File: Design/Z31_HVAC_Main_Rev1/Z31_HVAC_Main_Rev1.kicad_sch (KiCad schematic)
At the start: 23 parts, among them J1 Conn_01x05, J2 Conn_02x18_Odd_Even, J3 Conn_01x10_Male, J4 Conn_01x09_Male, U1 MEGA2560PRO, U2 MCP2515, U3 TJR1443, U4 ULN2003, U5 ULN2003, U6 ULN2003, U7 ULN2003, U8 NCV4276B, U9 ULN2003

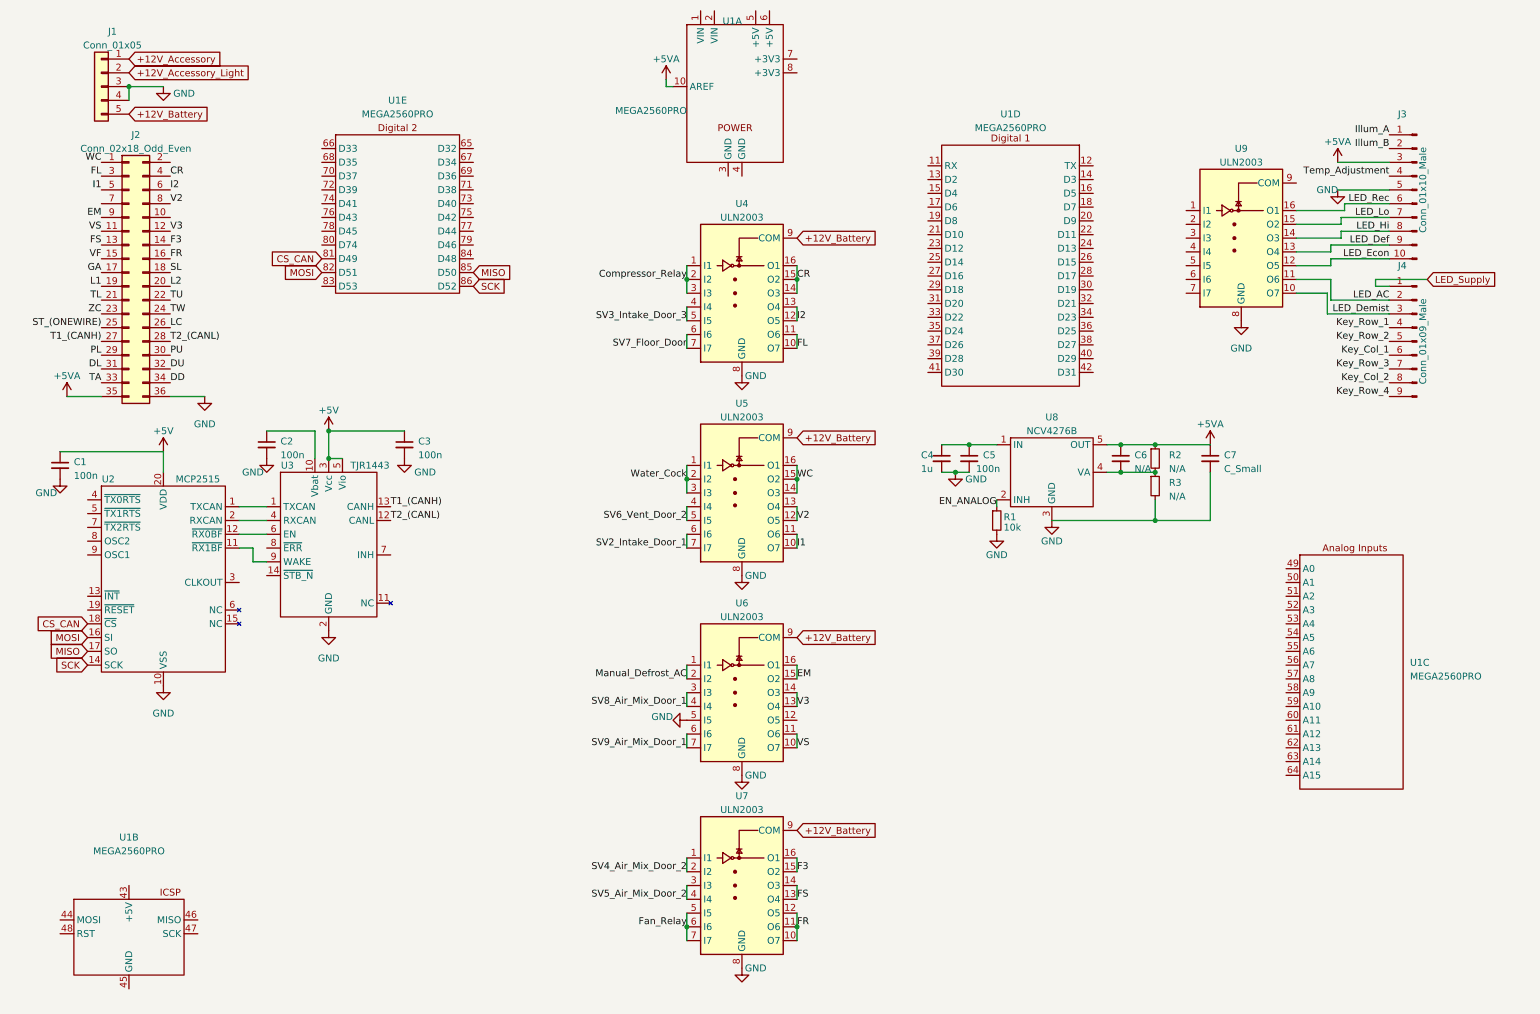
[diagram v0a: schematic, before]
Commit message: update to kicad-6
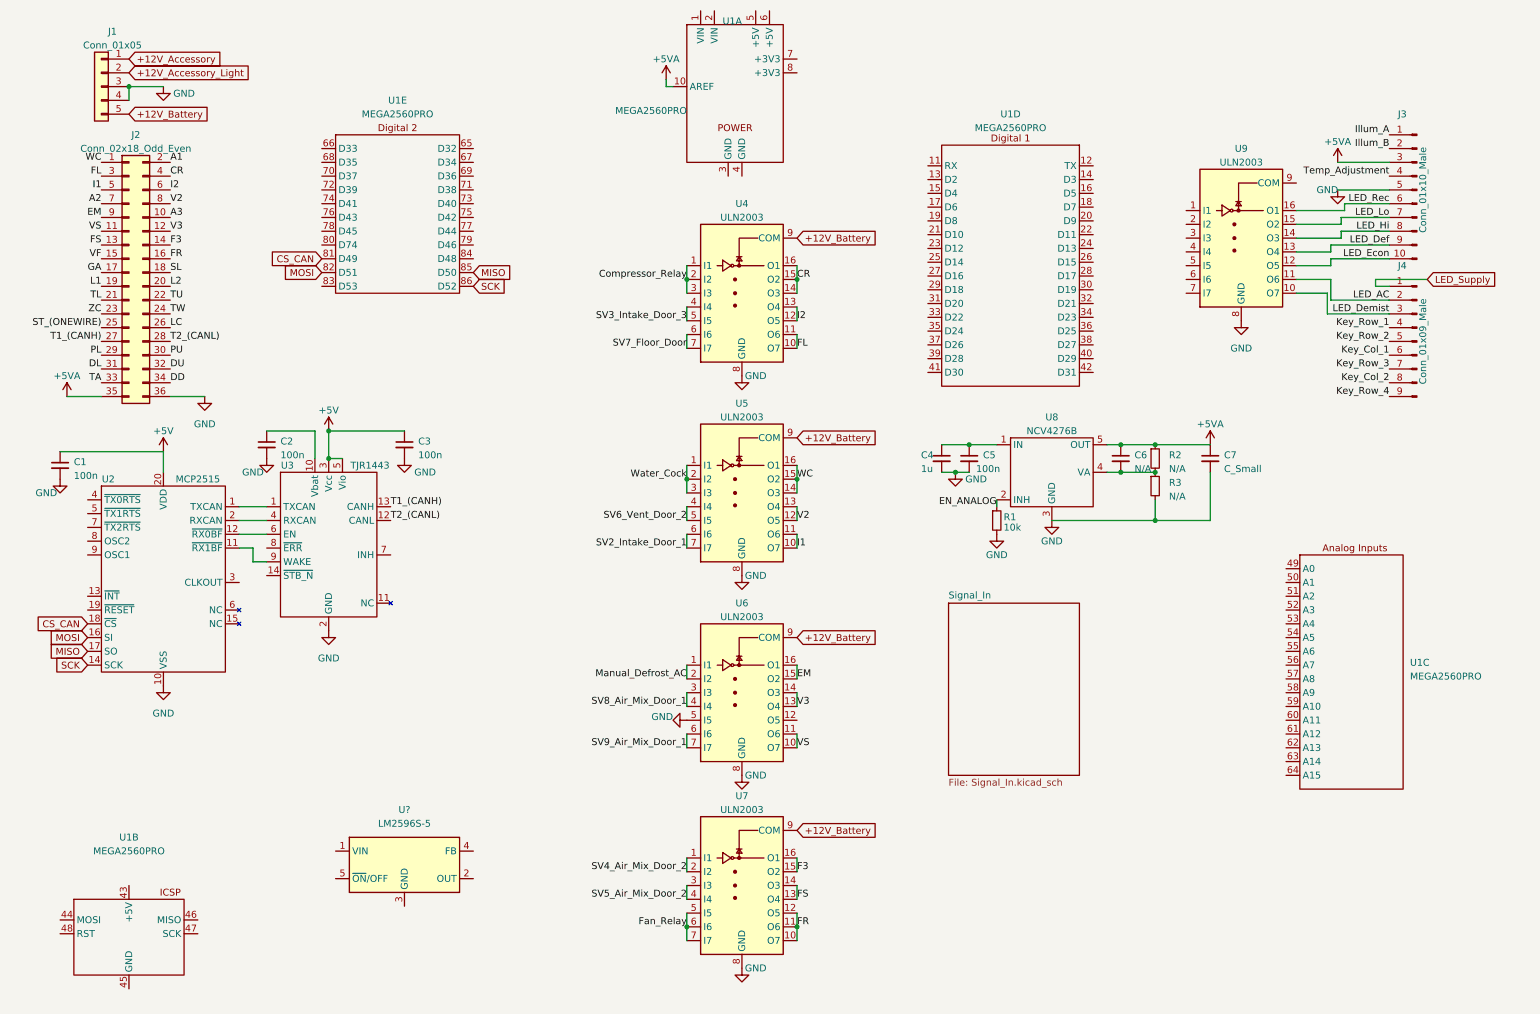
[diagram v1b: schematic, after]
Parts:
- added U?: LM2596S-5, Package_TO_SOT_SMD:TO-263-5_TabPin3, symbol Regulator_Switching:LM2596S-5
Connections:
- net A3: now reaches J2.10 (Pin_10)
- net A1: now reaches J2.2 (Pin_2)
- net A2: now reaches J2.7 (Pin_7)
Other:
- added sheet Signal_In (Signal_In.kicad_sch)

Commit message: afasdf
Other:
- added sheet Power_Drivers (Power_Drivers.kicad_sch)
- sheet Signal_In ports: added asfd, qwer; removed none
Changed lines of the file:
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@@
     (pin "2")
+  )
+  (sheet (at 212.09 123.19) (size 22.86 31.75) (fields_autoplaced)
+    (stroke (width 0.1524) (type solid) (color 0 0 0 0))
+    (fill (color 0 0 0 0.0000))
+    (property "Sheet name" "Power_Drivers" (id 0) (at 212.09 122.4784 0)
+      (effects (font (size 1.27 1.27)) (justify left bottom))
+    )
+    (property "Sheet file" "Power_Drivers.kicad_sch" (id 1) (at 212.09 155.5246 0)
+      (effects (font (size 1.27 1.27)) (justify left top))
+    )
   )
   (sheet (at 182.88 123.19) (size 24.13 31.75) (fields_autoplaced)
@@
       (effects (font (size 1.27 1.27)) (justify left top))
     )
+    (pin "asfd" input (at 182.88 128.27 180)
+      (effects (font (size 1.27 1.27)) (justify left))
+    )
+    (pin "qwer" input (at 182.88 130.81 180)
+      (effects (font (size 1.27 1.27)) (justify left))
+    )
   )
   (sheet_instances
     (path "/" (page "1"))
     (path "/ede5ba18-37cd-46ce-96ce-d6f4fa9c8fa9" (page "2"))
+    (path "/eb0c0d77-c260-4d94-b44a-6447b497255c" (page "3"))
   )
   (symbol_instances

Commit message: large changes
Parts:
- removed C4: 1u, Capacitor_SMD:C_1210_3225Metric_Pad1.33x2.70mm_HandSolder, symbol Device:C_Small
- removed C5: 100n, Capacitor_SMD:C_0805_2012Metric_Pad1.18x1.45mm_HandSolder, symbol Device:C_Small
- removed U4, U5, U6, U7: ULN2003, Package_SO:SO-16_3.9x9.9mm_P1.27mm, symbol Transistor_Array:ULN2003
- removed U8: NCV4276B, Package_TO_SOT_SMD:TO-263-5_TabPin3, symbol Personal:NCV4276B
- removed U?: LM2596S-5, Package_TO_SOT_SMD:TO-263-5_TabPin3, symbol Regulator_Switching:LM2596S-5
- added C1, C2: 20pF, Capacitor_SMD:C_0805_2012Metric_Pad1.18x1.45mm_HandSolder, symbol Device:C_Small
- added D1, D2: 1N4148, Diode_SMD:D_SOD-323_HandSoldering, symbol Device:D_Small
- added H1, H2: M3, MountingHole:MountingHole_3.5mm_Pad, symbol Mechanical:MountingHole_Pad
- added J1: Blower_Out, Connector_PinHeader_2.54mm:PinHeader_1x01_P2.54mm_Vertical, symbol Connector_Generic:Conn_01x01
- added J4: Analog_En, Connector_PinHeader_2.54mm:PinHeader_1x01_P2.54mm_Vertical, symbol Connector_Generic:Conn_01x01
- added J5: Blower_PWM, Connector_PinHeader_2.54mm:PinHeader_1x01_P2.54mm_Vertical, symbol Connector_Generic:Conn_01x01
- added J6: Conn_01x03, Personal:Proto-Area, symbol Connector_Generic:Conn_01x03
- added J7: Conn_01x18_Male, Connector_PinHeader_2.54mm:PinHeader_1x18_P2.54mm_Vertical, symbol Connector:Conn_01x18_Male
- added R10, R11, R12, R13, R14, R15, R16, R17, R18, R4, R5, R6, R7, R8, R9: 0R, Resistor_THT:R_Axial_DIN0204_L3.6mm_D1.6mm_P2.54mm_Vertical, symbol Device:R_Small
- added Y1: 8MHz, Crystal:Crystal_SMD_HC49-SD, symbol Device:Crystal
- C6: value N/A -> 100pF
- C7: value C_Small -> 100pF; footprint Capacitor_SMD:C_1210_3225Metric_Pad1.33x2.70mm_HandSolder -> Capacitor_SMD:C_0805_2012Metric_Pad1.18x1.45mm_HandSolder
- J2: footprint Personal:z31_hvac_connector_2 -> Personal:TE-172023
- J3: renamed from J1; footprint (none) -> Personal:Z31_HVAC_Connector_1
- R1: value 10k -> R_Small
- R2: value N/A -> R_Small
- R3: value N/A -> 100R; footprint Resistor_SMD:R_0805_2012Metric_Pad1.20x1.40mm_HandSolder -> Resistor_THT:R_Axial_DIN0207_L6.3mm_D2.5mm_P7.62mm_Horizontal
- U1: renamed from U2; symbol Personal:MCP2510 -> Interface_CAN_LIN:MCP2515-xST
- renumbered C1 to C3, C2 to C4, C3 to C5, J3 to J8, J4 to J9, U3 to U2, U1 to U3, U9 to U4
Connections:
- net Illum_A is gone; now on net L2: J8.1 (Pin_1)
- net Illum_B is gone; now on net L1: J8.2 (Pin_2)
- net LED_Supply is gone; now on net +12V: J9.1 (Pin_1)
- net +5V: now also U3.5 (+5V), U3.6 (+5V), J6.2 (Pin_2), J7.3 (Pin_3)
- net +5VA: no longer C6.1, C7.1, R2.1, U3.10 (AREF)
- net Compressor_Relay: now also U3.27 (D16)
- net Fan_Relay: now also U3.13 (D2)
- net GND: now also C6.2, R2.2, U3.3 (GND), U3.4 (GND), C1.1, C2.1, J6.1 (Pin_1), J7.1 (Pin_1), J7.18 (Pin_18), R4.1, R4.2; no longer R1.2, R3.2
- net Key_Col_1: now also U3.38 (D27)
- net Key_Col_2: now also U3.34 (D23)
- net Key_Row_1: now also U3.42 (D31)
- net Key_Row_2: now also U3.40 (D29)
- net Key_Row_3: now also U3.36 (D25)
- net Key_Row_4: now also U3.32 (D21)
- net MISO: now also R7.1
- net MOSI: now also R6.1
- net Manual_Defrost_AC: now also U3.18 (D7)
- net SCK: now also R5.1
- net SV2_Intake_Door_1: now also U3.22 (D11)
- net SV3_Intake_Door_3: now also U3.25 (D14)
- net SV4_Air_Mix_Door_2: now also U3.15 (D4)
- net SV5_Air_Mix_Door_2: now also U3.14 (D3)
- net SV6_Vent_Door_2: now also U3.21 (D10)
- net SV7_Floor_Door: now also U3.23 (D12)
- net SV8_Air_Mix_Door_1: now also U3.17 (D6)
- net SV9_Air_Mix_Door_1: now also U3.16 (D5)
- net VF: now also J1.1 (Pin_1)
- net Water_Cock: now also U3.26 (D15)
- net TXCAN: now reaches U1.1 (TXCAN), U2.1 (TXCAN)
- net at U2.9 (WAKE): now also R1.2, R2.1; no longer U1.11 (~{RX1BF})
- net TRJ1443EN: now reaches U1.12 (~{RX0BF})
- net TRJ1443EN: now also U2.14 (~{STB_N}); no longer U2.6 (EN)
- net INT_CAN: now reaches U1.13 (~{INT})
- net INT_CAN: now also U3.30 (D19)
- net RESET_CAN: now reaches U1.19 (~{RESET})
- net RESET_CAN: now also U3.76 (D43)
- net RXCAN: now reaches U1.2 (RXCAN), U2.4 (RXCAN)
- net TRJ1443ERR: now reaches U1.4 (~{TX0RTS})
- net TRJ1443ERR: now also U2.8 (~{ERR})
- net at U1.8 (OSC2): now also C1.2, Y1.1
- net at U1.9 (OSC1): now also C2.2, Y1.2
- net +12V: now reaches C4.1, U2.10 (Vbat)
- net +12V: now also J6.3 (Pin_3)
- net REG_INHIBIT: now reaches U2.7 (INH)
- net Signal_In (Analog)/Temp_In_Lower: now reaches U3.49 (A0)
- net Signal_In (Analog)/Lighting_Low: now reaches U3.50 (A1)
- net Signal_In (Analog)/Sun Load: now reaches U3.51 (A2)
- net Signal_In (Analog)/Temp_In_Upper: now reaches U3.52 (A3)
- net Signal_In (Analog)/Position_2: now reaches U3.53 (A4)
- net Signal_In (Analog)/Temp_Water: now reaches U3.54 (A5)
- net Signal_In (Analog)/Temp_Duct_Lower: now reaches U3.55 (A6)
- net Signal_In (Analog)/Position_1: now reaches U3.56 (A7)
- net Signal_In (Analog)/Temp_Ambient: now reaches U3.57 (A8)
- net Signal_In (Analog)/Temp_Duct_Upper: now reaches U3.58 (A9)
- net Signal_In (Analog)/Temp_Module: now reaches U3.59 (A10)
- net Signal_In (Analog)/Temp_Duct_Defrost: now reaches U3.60 (A11)
- net Signal_In (Analog)/Battery_Voltage: now reaches U3.61 (A12)
- net Signal_In (Analog)/A_Spare_1: now reaches U3.62 (A13)
- net Signal_In (Analog)/A_Spare_2: now reaches U3.63 (A14)
- net Signal_In (Analog)/Position_Split: now reaches U3.64 (A15)
- net Aux_3: now reaches U3.19 (D8)
- net Aux_2: now reaches U3.20 (D9)
- net Blower_Speed: now reaches U3.24 (D13)
- net Blower_Speed: now also J5.1 (Pin_1)
- net Aux_1: now reaches U3.28 (D17)
- net at U3.29 (D18): now also U4.1 (I1)
- net at U3.31 (D20): now also U4.2 (I2)
- net at U3.33 (D22): now also U4.3 (I3)
- net at U3.35 (D24): now also U4.4 (I4)
- net at U3.37 (D26): now also U4.5 (I5)
- net at U3.39 (D28): now also U4.6 (I6)
- net at U3.41 (D30): now also U4.7 (I7)
- net DAux1: now reaches U3.65 (D32)
- net DAux1: now also R18.1
- net Singal_In (Discrete)/Signal_Lighting: now reaches U3.66 (D33)
- net DAux2: now reaches U3.67 (D34)
- net DAux2: now also R17.1
- net Singal_In (Discrete)/Superheat_Timer: now reaches U3.68 (D35)
- net DAux3: now reaches U3.69 (D36)
- net DAux3: now also R16.1
- net Singal_In (Discrete)/Bulb_Check: now reaches U3.70 (D37)
- net DSC1: now reaches U3.71 (D38)
- net DSC1: now also R15.1
- net Ignition: now reaches U3.72 (D39)
- net DCS2: now reaches U3.73 (D40)
- net DCS2: now also R14.1
- net Singal_In (Discrete)/OneWire: now reaches U3.74 (D41)
- net DCS3: now reaches U3.75 (D42)
- net DCS3: now also R13.1
- net BL1: now reaches U3.77 (D44)
- net BL1: now also R12.1
- net BL2: now reaches U3.78 (D45)
- net BL2: now also R11.1
- net BL3: now reaches U3.79 (D46)
- net BL3: now also R10.1
- net RST: now reaches U3.80 (D74)
- net RST: now also R9.1
- net D/C: now reaches U3.84 (D48)
- net D/C: now also R8.1
- net +12V_Accessory renamed VA
- net VA: now also D1.2 (A)
- net +12V_Accessory_Light renamed LA
- net LA: now also D2.2 (A)
- net EN_ANALOG renamed +12V_Ignition
- net +12V_Ignition: now also R3.1
- new net: J7.11 (Pin_11), R12.2
- new net: J7.4 (Pin_4), R5.2
- new net: J7.17 (Pin_17), R18.2
- new net: J7.6 (Pin_6), R7.2
- new net: D1.1 (K), D2.1 (K), R3.2
- new net: J7.5 (Pin_5), R6.2
- new net: C7.1, H2.1
- new net: J7.9 (Pin_9), R10.2
- new net: J7.16 (Pin_16), R17.2
- new net: C6.1, H1.1
- new net: J7.10 (Pin_10), R11.2
- new net: J7.12 (Pin_12), R13.2
- new net: J7.13 (Pin_13), R14.2
- new net: J7.14 (Pin_14), R15.2
- new net: J7.15 (Pin_15), R16.2
- new net: J7.7 (Pin_7), R8.2
- new net: J7.8 (Pin_8), R9.2
- new net +3V3: J7.2 (Pin_2)
- new net Power/EN_Analog: J4.1 (Pin_1)
- new net TRJ1443_STB: U1.11 (~{RX1BF}), U2.6 (EN)
- no-connect marks 0 -> 5
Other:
- sheet Signal_In renamed Signal_In (Analog)
- added sheet Power (Power.kicad_sch)
- added sheet Singal_In (Discrete) (Discrete.kicad_sch)
- sheet Power_Drivers ports: added A1, A2, A3, Aux_1, Aux_2, Aux_3, COM, CR, Compressor_Relay, EM, F3, FL, FR, FS, Fan_Relay, I1, I2, Manual_Defrost_AC, SV2_Intake_Door_1, SV3_Intake_Door_3, SV4_Air_Mix_Door_2, SV5_Air_Mix_Door_2, SV6_Vent_Door_2, SV7_Floor_Door, SV8_Air_Mix_Door_1, SV9_Air_Mix_Door_1, V2, V3, VS, WC, Water_Cock; removed none
- sheet Signal_In (Analog) ports: added A_Spare_1, A_Spare_2, Battery_Voltage, DD, DL, DU, L1, Lighting_Low, PL, PU, Position_1, Position_2, Position_Split, Split, Sun Load, TA, TL, TU, TW, Temp_Ambient, Temp_Duct_Defrost, Temp_Duct_Lower, Temp_Duct_Upper, Temp_In_Lower, Temp_In_Upper, Temp_Module, Temp_Water, VB, ZC; removed asfd, qwer
- moved on the sheet: C3, C4, C5, J3, J8, J9, U2, U3A, U3B, U3C, U3D, U3E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
